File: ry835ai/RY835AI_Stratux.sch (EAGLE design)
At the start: 5 parts, among them X2 RASPI_BOARD_B+#_HD

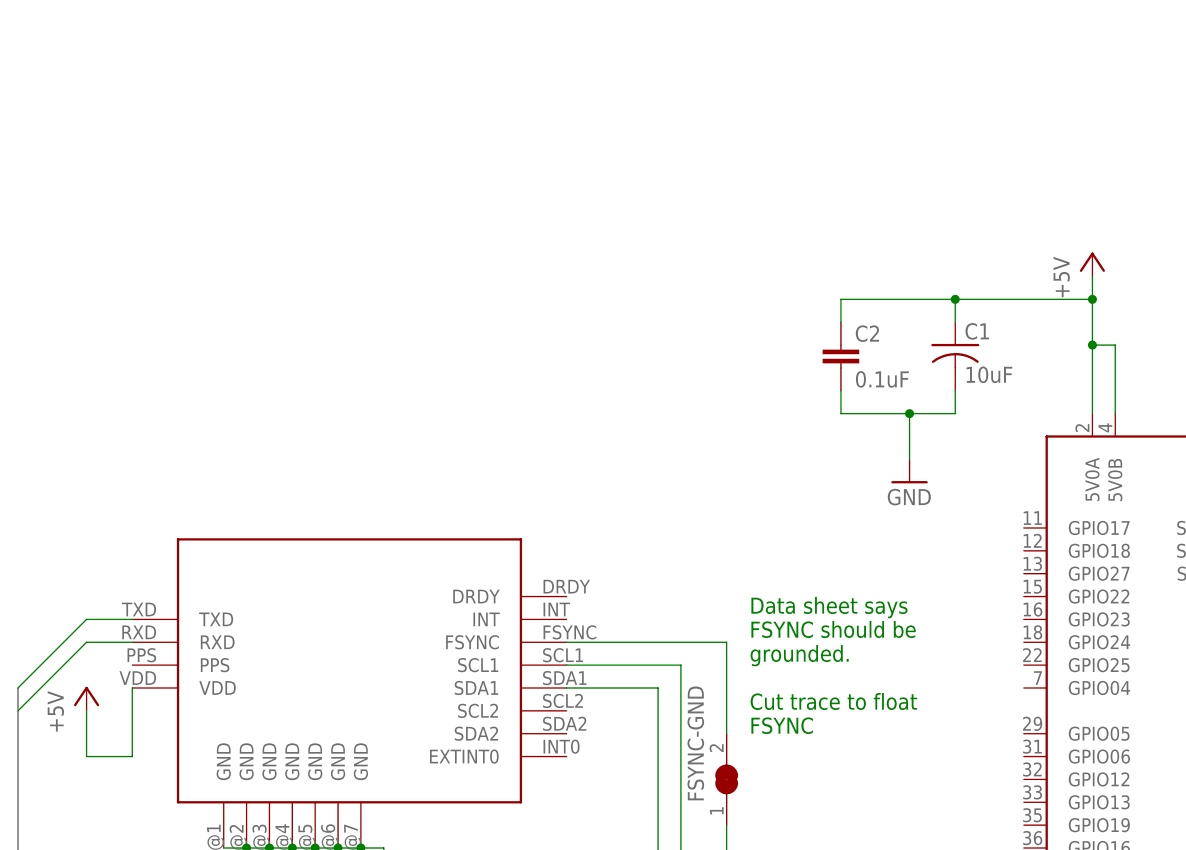
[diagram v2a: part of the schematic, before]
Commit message: added fan control
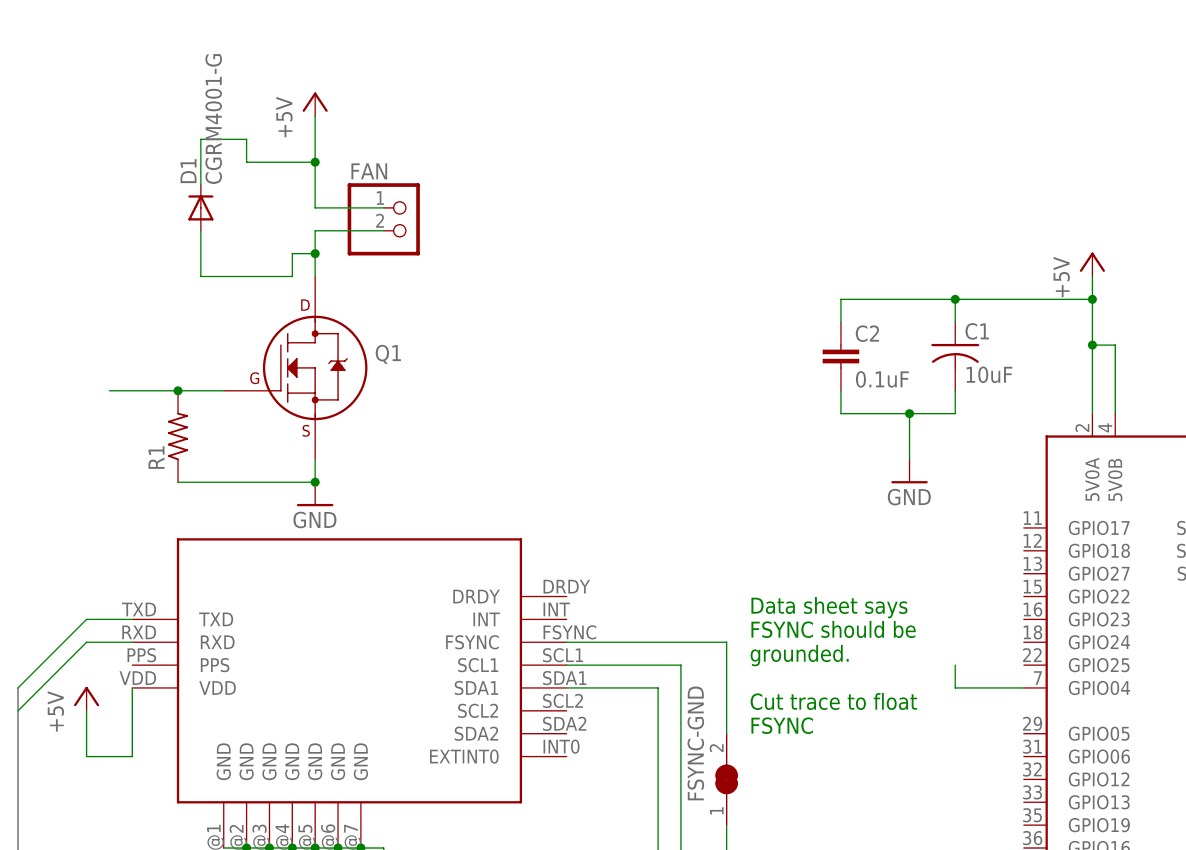
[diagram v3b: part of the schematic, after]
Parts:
- added D1: CGRM4001-G, diode:CGRM4001-G
- added FAN: (no value), pinhead:PINHD-1X2
- added Q1: (no value), transistors:2N7000_SOT23
- added R1: (no value), resistor:R-US_R0805
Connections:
- new net FAN_GPIO: Q1.G, R1.2, X2.GPIO04
- new net N$4: D1.A, FAN.2, Q1.D
- net +5V: now also D1.C, FAN.1
- net GND: now also Q1.S, R1.1
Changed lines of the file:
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@@
 <layer number="97" name="Info" color="7" fill="1" visible="yes" active="yes"/>
 <layer number="98" name="Guide" color="6" fill="1" visible="yes" active="yes"/>
+<layer number="99" name="SpiceOrder" color="5" fill="1" visible="yes" active="yes"/>
 <layer number="100" name="Muster" color="7" fill="1" visible="no" active="no"/>
 <layer number="101" name="Patch_Top" color="12" fill="4" visible="yes" active="yes"/>
@@
 <part name="FSYNC-GND" library="jblib" deviceset="CUTJUMPER" device=""/>
 <part name="X2" library="raspberrypi_bastelstube_v13" deviceset="RASPI_BOARD_B+#" device="_HD"/>
+<part name="Q1" library="transistors" deviceset="2N700*" device="_SOT23" technology="0"/>
+<part name="D1" library="diode" deviceset="CGRM400*-G" device="" technology="1"/>
+<part name="FAN" library="pinhead" deviceset="PINHD-1X2" device=""/>
+<part name="GND2" library="supply1" deviceset="GND" device=""/>
+<part name="P+3" library="supply1" deviceset="+5V" device=""/>
+<part name="R1" library="resistor" deviceset="R-US_" device="R0805"/>
 </parts>
 <sheets>
@@
 <instance part="FSYNC-GND" gate="1" x="96.52" y="33.02" rot="R90"/>
 <instance part="X2" gate="G$1" x="144.78" y="45.72"/>
+<instance part="Q1" gate="G$1" x="50.8" y="78.74"/>
+<instance part="D1" gate="G$1" x="38.1" y="96.52" rot="R90"/>
+<instance part="FAN" gate="G$1" x="60.96" y="93.98"/>
+<instance part="GND2" gate="1" x="50.8" y="63.5"/>
+<instance part="P+3" gate="1" x="50.8" y="109.22"/>
+<instance part="R1" gate="G$1" x="35.56" y="71.12" rot="R90"/>
 </instances>
 <busses>
@@
 <wire x1="96.52" y1="27.94" x2="96.52" y2="20.32" width="0.1524" layer="91"/>
 </segment>
+<segment>
+<pinref part="Q1" gate="G$1" pin="S"/>
+<pinref part="GND2" gate="1" pin="GND"/>
+<pinref part="R1" gate="G$1" pin="1"/>
+<wire x1="35.56" y1="66.04" x2="50.8" y2="66.04" width="0.1524" layer="91"/>
+<wire x1="50.8" y1="66.04" x2="50.8" y2="68.58" width="0.1524" layer="91"/>
+<junction x="50.8" y="66.04"/>
+</segment>
 </net>
 <net name="+5V" class="1">
@@
 <junction x="137.16" y="81.28"/>
 </segment>
+<segment>
+<pinref part="FAN" gate="G$1" pin="1"/>
+<wire x1="58.42" y1="96.52" x2="50.8" y2="96.52" width="0.1524" layer="91"/>
+<wire x1="50.8" y1="96.52" x2="50.8" y2="101.6" width="0.1524" layer="91"/>
+<pinref part="P+3" gate="1" pin="+5V"/>
+<wire x1="50.8" y1="101.6" x2="50.8" y2="106.68" width="0.1524" layer="91"/>
+<wire x1="38.1" y1="99.06" x2="38.1" y2="104.14" width="0.1524" layer="91"/>
+<wire x1="38.1" y1="104.14" x2="43.18" y2="104.14" width="0.1524" layer="91"/>
+<wire x1="43.18" y1="104.14" x2="43.18" y2="101.6" width="0.1524" layer="91"/>
+<wire x1="43.18" y1="101.6" x2="50.8" y2="101.6" width="0.1524" layer="91"/>
+<pinref part="D1" gate="G$1" pin="C"/>
+<junction x="50.8" y="101.6"/>
+</segment>
 </net>
 <net name="N$1" class="0">
@@
 </segment>
 </net>
+<net name="FAN_GPIO" class="0">
+<segment>
+<pinref part="Q1" gate="G$1" pin="G"/>
+<wire x1="40.64" y1="76.2" x2="35.56" y2="76.2" width="0.1524" layer="91"/>
+<pinref part="R1" gate="G$1" pin="2"/>
+<wire x1="35.56" y1="76.2" x2="27.94" y2="76.2" width="0.1524" layer="91"/>
+<junction x="35.56" y="76.2"/>
+</segment>
+<segment>
+<pinref part="X2" gate="G$1" pin="GPIO04"/>
+<wire x1="129.54" y1="43.18" x2="121.92" y2="43.18" width="0.1524" layer="91"/>
+<wire x1="121.92" y1="43.18" x2="121.92" y2="45.72" width="0.1524" layer="91"/>
+</segment>
+</net>
+<net name="N$4" class="0">
+<segment>
+<pinref part="Q1" gate="G$1" pin="D"/>
+<wire x1="50.8" y1="88.9" x2="50.8" y2="91.44" width="0.1524" layer="91"/>
+<pinref part="FAN" gate="G$1" pin="2"/>
+<wire x1="50.8" y1="91.44" x2="50.8" y2="93.98" width="0.1524" layer="91"/>
+<wire x1="50.8" y1="93.98" x2="58.42" y2="93.98" width="0.1524" layer="91"/>
+<wire x1="38.1" y1="93.98" x2="38.1" y2="88.9" width="0.1524" layer="91"/>
+<wire x1="38.1" y1="88.9" x2="48.26" y2="88.9" width="0.1524" layer="91"/>
+<wire x1="48.26" y1="88.9" x2="48.26" y2="91.44" width="0.1524" layer="91"/>
+<wire x1="48.26" y1="91.44" x2="50.8" y2="91.44" width="0.1524" layer="91"/>
+<pinref part="D1" gate="G$1" pin="A"/>
+<junction x="50.8" y="91.44"/>
+</segment>
+</net>

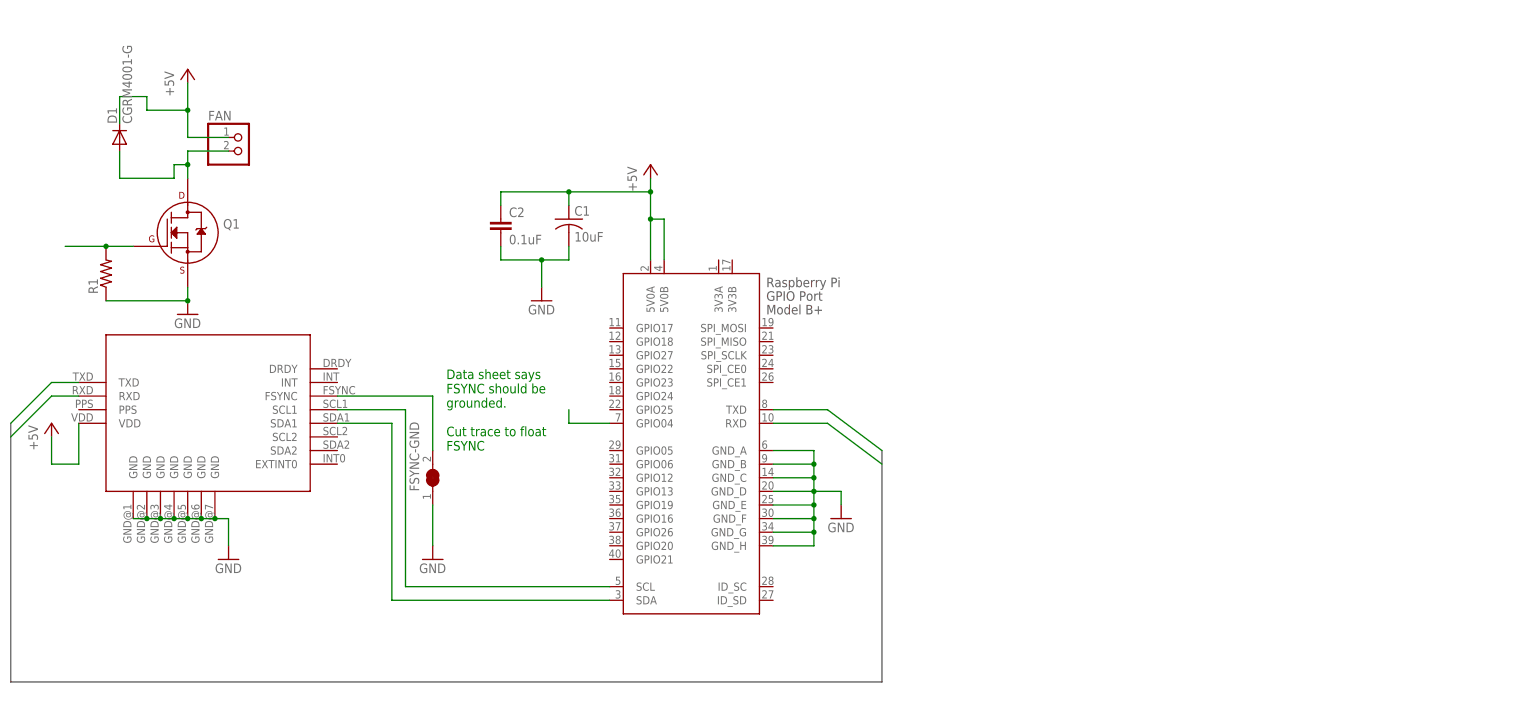
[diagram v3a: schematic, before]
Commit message: Revised board design with provisions for FAN & PWR_IN.
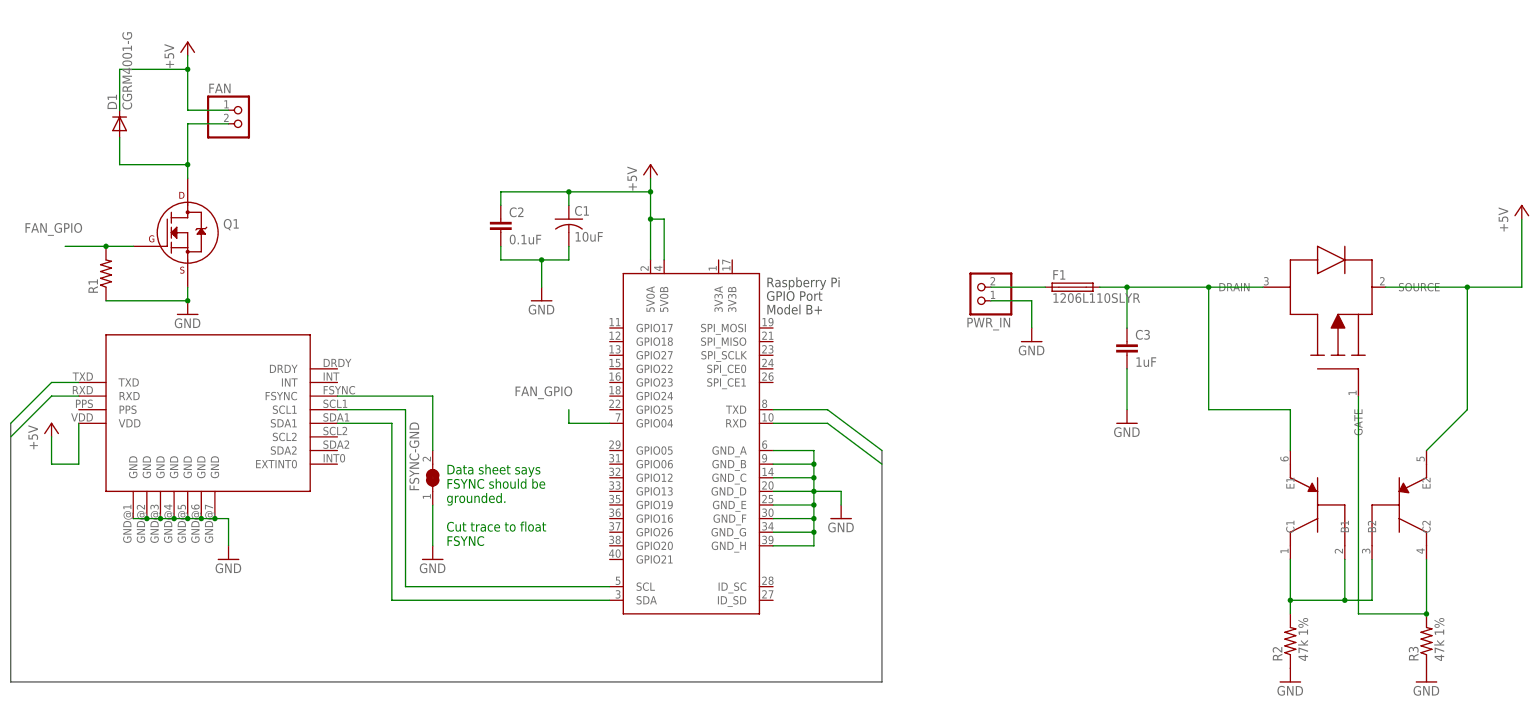
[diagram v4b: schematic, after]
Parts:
- added C3: 1uF, rcl:C-EUC0805
- added F1: 1206L110SLYR, jblib:FUSE
- added PWR_IN: (no value), pinhead:PINHD-1X2
- added R2, R3: 47k 1%, resistor:R-US_R0805
- added U$2: DMG2305UX, jblib:DMG2305UX
- added U$3: DMMT5401, jblib:DMMT5401
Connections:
- new net N$10: R3.2, U$2.GATE, U$3.C2
- new net N$6: F1.1, PWR_IN.2
- new net N$7: C3.1, F1.2, U$2.DRAIN, U$3.E1
- new net N$9: R2.2, U$3.B1, U$3.B2, U$3.C1
- net +5V: now also U$2.SOURCE, U$3.E2
- net GND: now also C3.2, PWR_IN.1, R2.1, R3.1
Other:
- moved on the sheet: D1, FAN

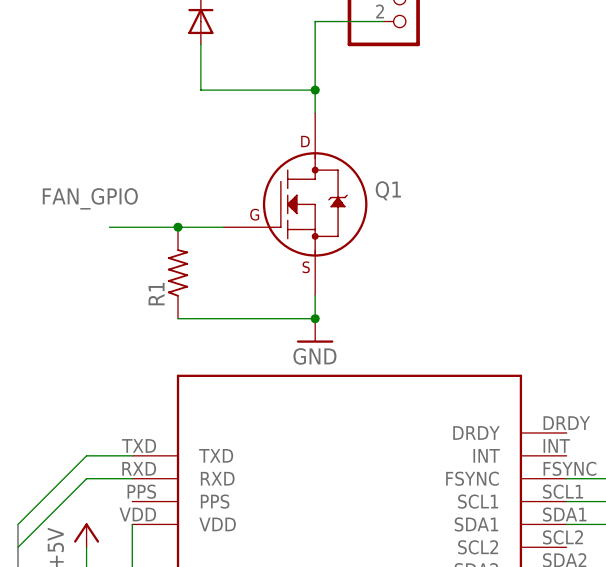
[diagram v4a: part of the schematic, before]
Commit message: Minor change R1=10k
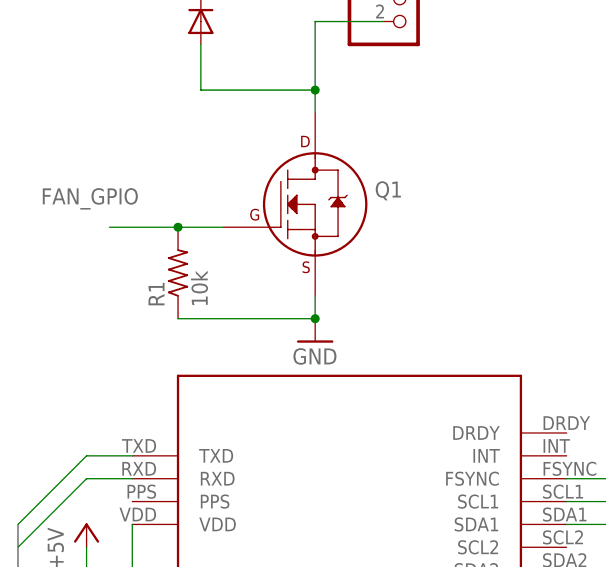
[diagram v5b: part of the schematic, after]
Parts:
- R1: value (none) -> 10k
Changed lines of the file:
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@@
 <part name="GND2" library="supply1" deviceset="GND" device=""/>
 <part name="P+3" library="supply1" deviceset="+5V" device=""/>
-<part name="R1" library="resistor" deviceset="R-US_" device="R0805"/>
+<part name="R1" library="resistor" deviceset="R-US_" device="R0805" value="10k"/>
 <part name="F1" library="jblib" deviceset="FUSE" device="" value="1206L110SLYR"/>
 <part name="GND6" library="supply1" deviceset="GND" device=""/>

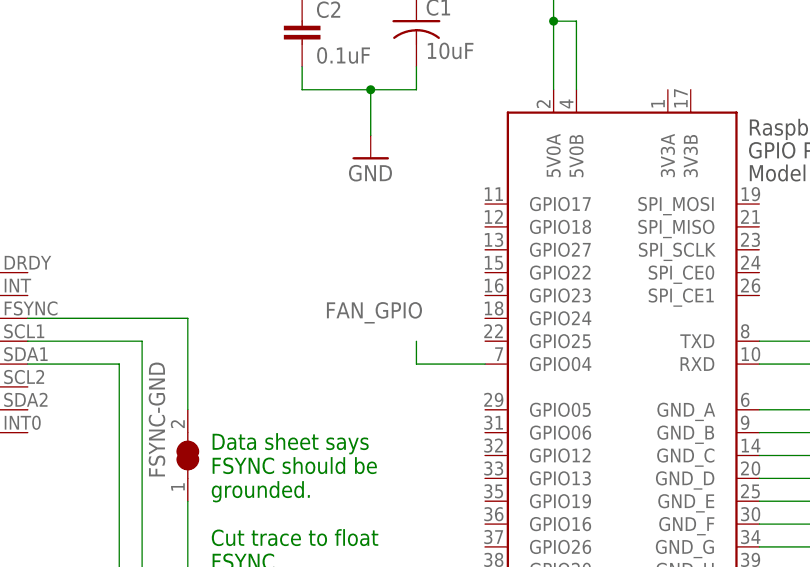
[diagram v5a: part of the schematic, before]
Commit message: Modified fan control signal to use GPIO18 rather than GPIO4. This is consistent with currently used AHRS boards. This revision has not been manufactured or tested, so make sure to DRC and double check if you decide to have this made.
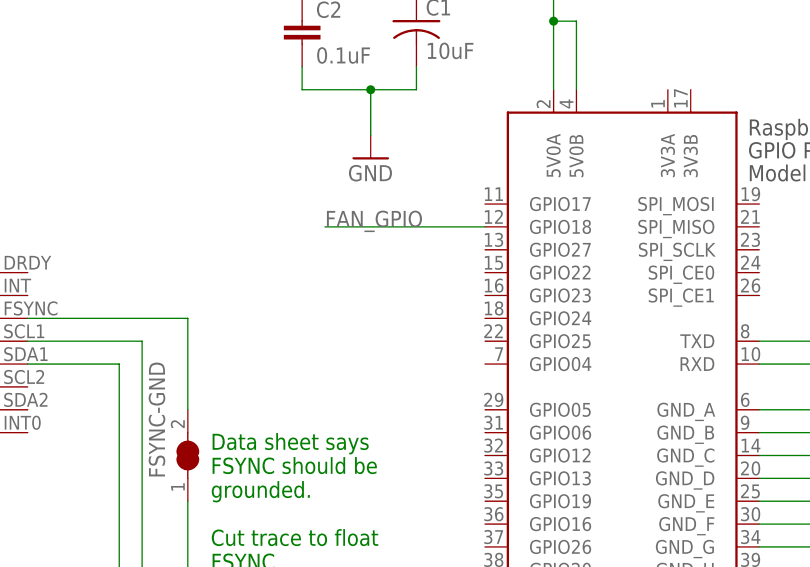
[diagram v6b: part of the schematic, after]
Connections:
- net FAN_GPIO: now also X2.GPIO18; no longer X2.GPIO04
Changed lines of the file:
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@@
 <?xml version="1.0" encoding="utf-8"?>
 <!DOCTYPE eagle SYSTEM "eagle.dtd">
-<eagle version="7.2.0">
+<eagle version="8.2.1">
 <drawing>
 <settings>
@@
 </segment>
 <segment>
-<pinref part="X2" gate="G$1" pin="GPIO04"/>
-<wire x1="129.54" y1="43.18" x2="121.92" y2="43.18" width="0.1524" layer="91"/>
-<wire x1="121.92" y1="43.18" x2="121.92" y2="45.72" width="0.1524" layer="91"/>
-<label x="111.76" y="48.26" size="1.778" layer="95"/>
-</segment>
-</net>
+<pinref part="X2" gate="G$1" pin="GPIO18"/>
+<wire x1="129.54" y1="58.42" x2="111.76" y2="58.42" width="0.1524" layer="91"/>
+<label x="111.76" y="58.42" size="1.778" layer="95"/>
+</segment>
+</net>
